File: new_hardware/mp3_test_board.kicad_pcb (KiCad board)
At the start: 4 copper layers, 100 x 56 mm, 199 parts, among them J1 TF01-A, J2 PJ-322, P1 WF24LTYAJDNN0#, P2 USB-TYPE-C-018, Q1 2N7002K, SW1 K2-1156SP-F5SW-05, SW2 K2-1156SP-F5SW-05, SW3 K2-1156SP-F5SW-05, SW4 K2-1156SP-F5SW-05, SW5 K2-1156SP-F5SW-05, SW6 GT-TC054A-H035-L1, SW7 GT-TC054A-H035-L1, SW8 GT-TC054A-H035-L1, U1 F133, U10 SGM6603-ADJYN6G, U11 SGM3204, U2 USBLC6-2SC6, U3 MX25L25645GM2I-08G, U4 PCM1795, U5 LM4562, U6 LM4562, U7 OPA1656, U8 OPA1656, U9 AXP2101, Y1 12.88727

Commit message: some fucking changes
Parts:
- removed C56, C59, C60: 0.1u, rlib_passive:C_0603_1608Metric
- removed C66: 10u, rlib_passive:C_0603_1608Metric
- removed L1, L5, L6: L, rlib_passive:INDC2520X120N
- added D13: PESD3V3L1BA, rlib_passive:D_SOD-323F, B.Cu at (123.8, 47.2)
- added D14: PESD3V3L1BA, rlib_passive:D_SOD-323F, B.Cu at (117.0, 47.0)
- added FB1: FerriteBead, rlib_passive:INDC2520X120N, B.Cu at (159.3, 48.2)
- added FB2: FerriteBead, rlib_passive:INDC2520X120N, B.Cu at (168.5, 77.6)
- added FB3: FerriteBead, rlib_passive:INDC2520X120N, B.Cu at (165.1, 62.8)
- added NT1: NetTie_2, NetTie:NetTie-2_SMD_Pad2.0mm, F.Cu at (160.1, 103.6)
- added R51: 27, rlib_passive:R_0603_1608Metric, B.Cu at (121.4, 47.0)
- added R52: 27, rlib_passive:R_0603_1608Metric, B.Cu at (119.2, 47.0)
- added R53: 10k, rlib_passive:R_0603_1608Metric, B.Cu at (105.0, 62.0)
- added R54: 0, rlib_passive:R_0603_1608Metric, B.Cu at (147.9, 45.2)
- added R55: 0, rlib_passive:R_0603_1608Metric, B.Cu at (149.8, 45.2)
- added R56: 10k, rlib_passive:R_0603_1608Metric, B.Cu at (110.6, 46.2)
- added R57: 10k, rlib_passive:R_0603_1608Metric, B.Cu at (110.6, 44.2)
- added U12: AP6212, rlib_modules:QFN-44_L12.0-W12.0-P0.90-TL_AP6212, F.Cu at (122.1, 111.0)
- C32, C33: footprint rlib_passive:R_0603_1608Metric -> rlib_passive:C_0603_1608Metric
- C34, C35, C45, C46, C55: value 0.1u -> 100n
- C51, C52, R10, R11, R7, R9: moved to B.Cu
- R47: value R -> 100k
- R48: value R -> 11k
- R6: value 50 -> 100
- moved R39 130.9 mm to (147.6, 75.8), turned to 0 degrees
- moved R35 116.2 mm to (144.8, 76.6), turned to 90 degrees
- moved R49 103.4 mm to (153.6, 49.4), turned to 0 degrees
- moved TP13 99.8 mm to (154.8, 95.2)
- moved TP15 90.8 mm to (155.6, 46.6)
- moved C52 89.4 mm to (150.4, 80.6), turned to 90 degrees
- moved C51 88.8 mm to (150.4, 76.5), turned to 90 degrees
- moved R50 85.9 mm to (152.2, 47.2), turned to 90 degrees
- moved R36 80.2 mm to (144.8, 80.7), turned to 90 degrees
- moved R40 78.9 mm to (147.7, 81.7), turned to 0 degrees
- moved R46 78.4 mm to (165.0, 69.8), turned to 0 degrees
- moved R20 74.3 mm to (164.6, 53.4)
- moved TP19 73.9 mm to (171.3, 80.8)
- moved R7 73.1 mm to (156.3, 60.0), turned to 180 degrees
- moved R19 71.6 mm to (164.7, 59.4)
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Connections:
- C16 pad 1: +0V9 -> -5VA
- C16 pad 2: GND -> GNDA
- C20 pad 1: Net-(C20-Pad1) -> GNDA
- C20 pad 2: GND -> +5VA
- C3 pad 1: +1V8A -> /SOC/KEYS
- C34 pad 1: GNDA -> -5VA
- C34 pad 2: +5VA -> GNDA
- C35 pad 1: -5VA -> GNDA
- C35 pad 2: GNDA -> +5VA
- C45 pad 1: GNDA -> -5VA
- C45 pad 2: +5VA -> GNDA
- C46 pad 1: -5VA -> GNDA
- C46 pad 2: GNDA -> +5VA
- C55 pad 1: GNDA -> -5VA
- C55 pad 2: +5VA -> GNDA
- C62 pad 1: Net-(C62-Pad1) -> VBUS
- C7 pad 1: +1V8A -> GNDA
- C7 pad 2: GND -> +5VA
- D1 pad 2: Net-(C20-Pad1) -> /SOC/KEYS
- P1 pad 22: unconnected-(P1-Pad22) -> GND
- P1 pad 30: Net-(P1-Pad30) -> /SOC/LCD_EN
- P1 pad 34: unconnected-(P1-Pad34) -> GND
- P1 pad 35: unconnected-(P1-Pad35) -> GND
- R13 pad 2: Net-(C20-Pad1) -> Net-(R13-Pad2)
- R16 pad 2: /SOC/SDC_D0 -> /SOC/SDC_CMD
- R18 pad 2: /SOC/SDC_D1 -> /SOC/SDC_CLK
- R3 pad 1: Net-(P1-Pad30) -> /SOC/LCD_EN
- SW7 pad 1: Net-(C20-Pad1) -> Net-(R13-Pad2)
- TP10 pad 1: DEBUG_UART_TX -> Net-(D14-Pad2)
- TP9 pad 1: DEBUG_UART_RX -> Net-(D13-Pad2)
- U1 pad 1: /SOC/SDC_PLUG -> unconnected-(U1-Pad1)
- U1 pad 10: unconnected-(U1-Pad10) -> /SOC/SDC_CMD
- U1 pad 11: unconnected-(U1-Pad11) -> /SOC/SDC_D3
- U1 pad 118: /SOC/SDC_CMD -> unconnected-(U1-Pad118)
- U1 pad 119: /SOC/SDC_D0 -> unconnected-(U1-Pad119)
- U1 pad 12: unconnected-(U1-Pad12) -> /SOC/SDC_D2
- U1 pad 120: /SOC/SDC_CLK -> unconnected-(U1-Pad120)
- U1 pad 121: /SOC/SDC_D1 -> unconnected-(U1-Pad121)
- U1 pad 122: /SOC/SDC_D3 -> unconnected-(U1-Pad122)
- U1 pad 123: /SOC/SDC_D2 -> unconnected-(U1-Pad123)
- U1 pad 124: /NewDAC/I2S_LRCK -> unconnected-(U1-Pad124)
- U1 pad 125: /NewDAC/I2S_BCLK -> unconnected-(U1-Pad125)
- U1 pad 127: /NewDAC/I2S_DIN -> unconnected-(U1-Pad127)
- U1 pad 2: /SOC/LCD_EN -> unconnected-(U1-Pad2)
- U1 pad 3: /NewDAC/I2C_SDIN -> unconnected-(U1-Pad3)
- U1 pad 31: /Power/IRQ -> unconnected-(U1-Pad31)
- U1 pad 32: unconnected-(U1-Pad32) -> /Power/IRQ
- U1 pad 38: unconnected-(U1-Pad38) -> /SOC/LCD_PWM
- U1 pad 4: /NewDAC/I2C_SCL -> unconnected-(U1-Pad4)
- U1 pad 47: unconnected-(U1-Pad47) -> Net-(R53-Pad1)
- U1 pad 5: /SOC/LCD_PWM -> unconnected-(U1-Pad5)
- U1 pad 52: unconnected-(U1-Pad52) -> /SOC/LCD_EN
- U1 pad 6: /NewDAC/I2S_MCLK -> /SOC/SDC_PLUG
- U1 pad 7: unconnected-(U1-Pad7) -> /SOC/SDC_D1
- U1 pad 79: unconnected-(U1-Pad79) -> /NewDAC/I2S_MCLK
- U1 pad 8: unconnected-(U1-Pad8) -> /SOC/SDC_D0
- U1 pad 80: unconnected-(U1-Pad80) -> /NewDAC/I2S_LRCK
- U1 pad 82: /SOC/LCD_D9 -> /NewDAC/I2S_BCLK
- U1 pad 84: /SOC/LCD_D8 -> /NewDAC/I2S_DIN
- U1 pad 85: /SOC/LCD_D1 -> /NewDAC/I2C_SDIN
- U1 pad 86: /SOC/LCD_D0 -> /NewDAC/I2C_SCL
- U1 pad 9: unconnected-(U1-Pad9) -> /SOC/SDC_CLK
- U9 pad 11: Net-(C66-Pad1) -> unconnected-(U9-Pad11)
- U9 pad 37: Net-(C62-Pad1) -> VBUS
- U9 pad 6: unconnected-(U9-Pad6) -> Net-(R54-Pad2)
- U9 pad 7: unconnected-(U9-Pad7) -> Net-(R55-Pad2)
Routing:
- net +5VA: track 10.3 -> 160.1 mm, vias 0 -> 10
- net /NewDAC/I2C_SDIN: track 3.83 -> 128.8 mm, vias 0 -> 6
- net -5VA: track 10.2 -> 135.1 mm, vias 0 -> 7
- net /NewDAC/I2C_SCL: track 3.30 -> 127.4 mm, vias 0 -> 6
- net /SOC/KEYS: track 36.8 -> 139.2 mm, vias 0 -> 2
- net GNDA: track 11.6 -> 113.2 mm, vias 3 -> 24
- net Net-(D12-Pad1): track 0.00 -> 99.4 mm, vias 0 -> 5
- net GND: track 90.0 -> 189.1 mm, vias 49 -> 81
- net +0V9: track 216.0 -> 139.6 mm, vias 4 -> 7
- net /SOC/USB_DM: track 53.6 -> 118.5 mm, vias 2 -> 4
- net /SOC/USB_DP: track 55.5 -> 112.1 mm, vias 2 -> 4
- net +3V3: track 296.9 -> 351.6 mm, vias 18 -> 20
- net Net-(C49-Pad2): track 10.1 -> 52.9 mm, vias 0 -> 2
- net VBUS: track 0.00 -> 42.6 mm, vias 0 -> 3
- net VCC: track 11.3 -> 49.0 mm, vias 0 -> 4
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- added copper zone on B.Cu, net +0V9
- added copper zone on B.Cu, net +3V3
- added copper zone on B.Cu, net GND
- added copper zone on In2.Cu, net GNDA

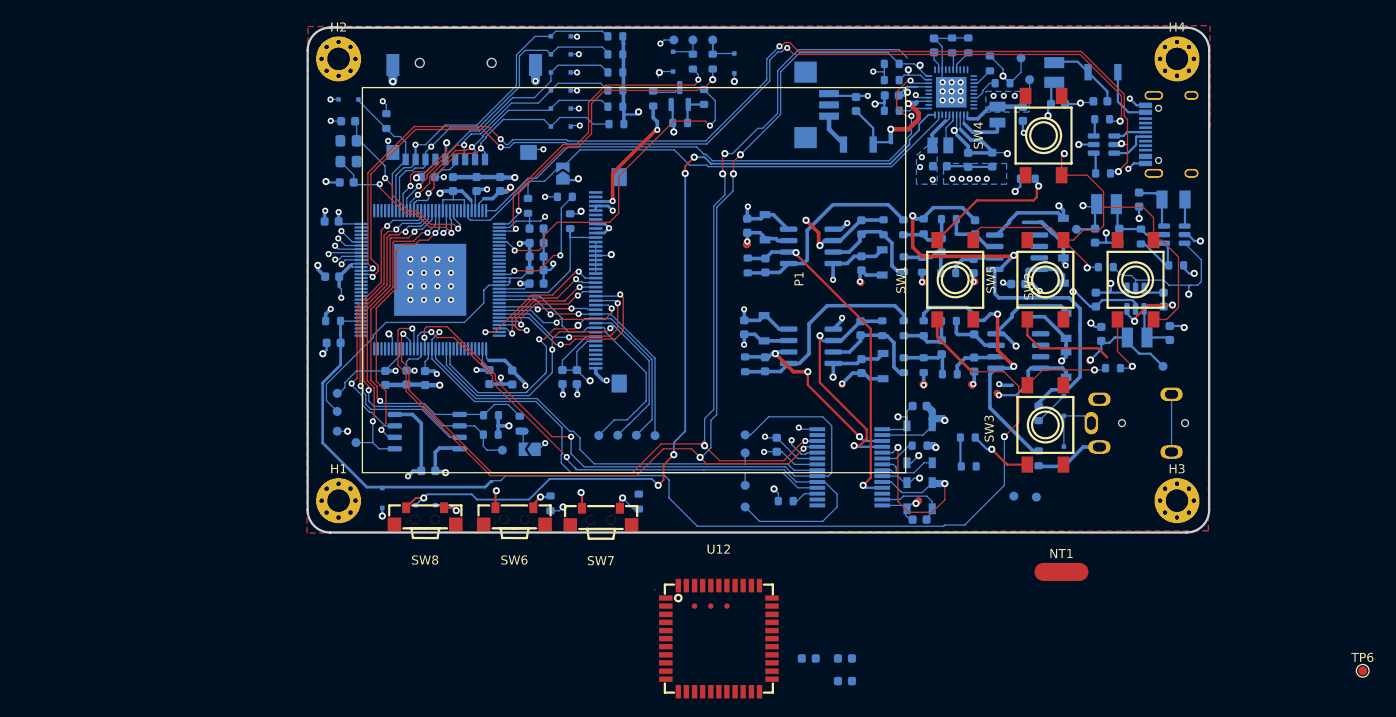
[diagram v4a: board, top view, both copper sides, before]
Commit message: device tree is changed
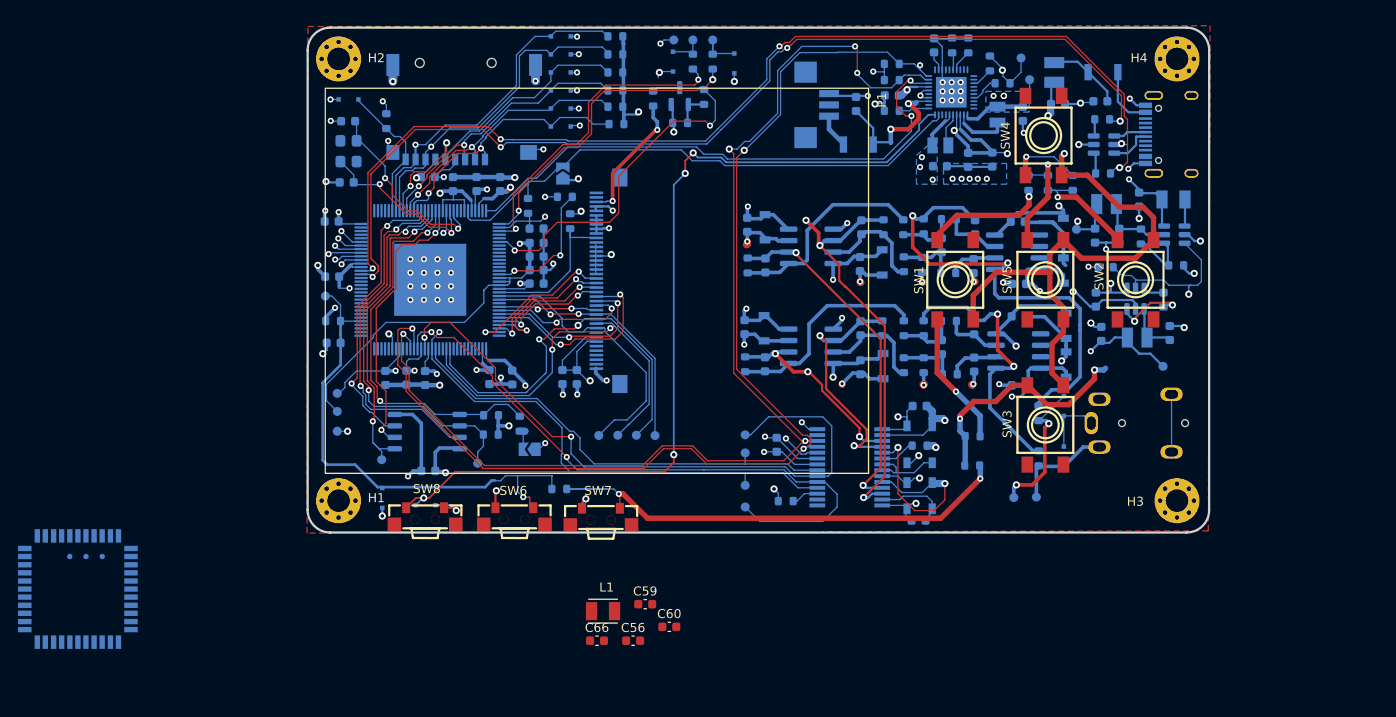
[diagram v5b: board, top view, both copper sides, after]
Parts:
- removed NT1: NetTie_2, NetTie:NetTie-2_SMD_Pad2.0mm
- added C56: 10u, rlib_passive:C_0603_1608Metric, F.Cu at (112.6, 111.2)
- added C59: 10u, rlib_passive:C_0603_1608Metric, F.Cu at (113.9, 107.2)
- added C60: 10u, rlib_passive:C_0603_1608Metric, F.Cu at (116.6, 109.7)
- added C66: 100n, rlib_passive:C_0603_1608Metric, F.Cu at (108.6, 111.2)
- added L1: 4.7u, rlib_passive:IND_LQH32PN4R7NN0L, F.Cu at (109.2, 108.0)
- R41, R42: value 50 -> 51
- TP6: moved to B.Cu
- U: renamed from U12; moved to B.Cu
- moved TP6 122.3 mm to (78.4, 73.0), turned to 180 degrees
- moved U 71.3 mm to (51.0, 105.5), turned to 180 degrees
- moved R12 65.6 mm to (158.6, 60.5), turned to -90 degrees
- moved R7 62.3 mm to (104.4, 94.4), turned to 0 degrees
- moved R13 59.7 mm to (161.3, 60.5), turned to 90 degrees
- moved C16 49.3 mm to (125.2, 65.1), turned to -90 degrees
- moved C7 44.1 mm to (137.7, 69.5), turned to 90 degrees
- moved C20 34.9 mm to (137.8, 80.9), turned to 90 degrees
- moved R11 32.1 mm to (156.4, 60.5), turned to 90 degrees
- moved C46 31.1 mm to (155.3, 82.9), turned to 0 degrees
- moved C35 30.8 mm to (155.4, 71.7), turned to 0 degrees
- moved C45 23.6 mm to (155.2, 64.8), turned to 0 degrees
- moved R9 19.0 mm to (150.2, 91.8)
- moved C34 14.8 mm to (124.9, 76.5), turned to -90 degrees
- moved P1 4.12 mm to (138.7, 92.7)
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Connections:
- C16 pad 2: GNDA -> GND
- C20 pad 1: GNDA -> GND
- C29 pad 2: GNDA -> GND
- C30 pad 1: GNDA -> GND
- C32 pad 2: GNDA -> GND
- C33 pad 2: GNDA -> GND
- C34 pad 2: GNDA -> GND
- C35 pad 1: GNDA -> GND
- C36 pad 2: GNDA -> GND
- C37 pad 2: GNDA -> GND
- C38 pad 2: GNDA -> GND
- C39 pad 2: GNDA -> GND
- C40 pad 1: GNDA -> GND
- C45 pad 2: GNDA -> GND
- C46 pad 1: GNDA -> GND
- C50 pad 1: GNDA -> GND
- C52 pad 1: GNDA -> GND
- C53 pad 2: GNDA -> GND
- C54 pad 1: GNDA -> GND
- C55 pad 2: GNDA -> GND
- C57 pad 2: GNDA -> GND
- C58 pad 1: GNDA -> GND
- C69 pad 2: GNDA -> GND
- C7 pad 1: GNDA -> GND
- C70 pad 2: GNDA -> GND
- C72 pad 2: GNDA -> GND
- C73 pad 2: GNDA -> GND
- C74 pad 2: GNDA -> GND
- C75 pad 2: GNDA -> GND
- D10 pad 1: GNDA -> GND
- D9 pad 1: GNDA -> GND
- J2 pad 1: GNDA -> GND
- P1 pad 40: (no net) -> unconnected-(P1-Pad40)
- R24 pad 2: GNDA -> GND
- R34 pad 1: GNDA -> GND
- R36 pad 1: GNDA -> GND
- R48 pad 1: GNDA -> GND
- SW1 pad 1: /SOC/KEYS -> Net-(R10-Pad2)
- SW1 pad 2: /SOC/KEYS -> Net-(R10-Pad2)
- SW1 pad 4: GND -> unconnected-(SW1-Pad4)
- SW2 pad 1: Net-(R7-Pad2) -> Net-(R12-Pad2)
- SW2 pad 2: Net-(R7-Pad2) -> Net-(R12-Pad2)
- SW3 pad 4: GND -> unconnected-(SW3-Pad4)
- SW4 pad 1: Net-(R10-Pad2) -> Net-(R13-Pad2)
- SW4 pad 2: Net-(R10-Pad2) -> Net-(R13-Pad2)
- SW6 pad 1: Net-(R12-Pad2) -> /SOC/KEYS
- SW7 pad 1: Net-(R13-Pad2) -> Net-(R7-Pad2)
- U pad 1: unconnected-(U12-Pad1) -> GND
- U pad 14: unconnected-(U12-Pad14) -> /SOC/WIFI_SDIO_D2
- U pad 15: unconnected-(U12-Pad15) -> /SOC/WIFI_SDIO_D3
- U pad 16: unconnected-(U12-Pad16) -> /SOC/WIFI_SDIO_CMD
- U pad 17: unconnected-(U12-Pad17) -> /SOC/WIFI_SDIO_CLK
- U pad 18: unconnected-(U12-Pad18) -> /SOC/WIFI_SDIO_D0
- U pad 19: unconnected-(U12-Pad19) -> /SOC/WIFI_SDIO_D1
- U pad 20: unconnected-(U12-Pad20) -> GND
- U pad 21: unconnected-(U12-Pad21) -> Net-(L1-Pad1)
- U pad 22: unconnected-(U12-Pad22) -> +3V3
- U pad 23: unconnected-(U12-Pad23) -> +3V3
- U pad 3: unconnected-(U12-Pad3) -> GND
- U pad 31: unconnected-(U12-Pad31) -> GND
- U pad 33: unconnected-(U12-Pad33) -> GND
- U pad 36: unconnected-(U12-Pad36) -> GND
- U pad 9: unconnected-(U12-Pad9) -> +3V3
- U1 pad 118: unconnected-(U1-Pad118) -> /SOC/WIFI_SDIO_CMD
- U1 pad 119: unconnected-(U1-Pad119) -> /SOC/WIFI_SDIO_D0
- U1 pad 120: unconnected-(U1-Pad120) -> /SOC/WIFI_SDIO_CLK
- U1 pad 121: unconnected-(U1-Pad121) -> /SOC/WIFI_SDIO_D1
- U1 pad 122: unconnected-(U1-Pad122) -> /SOC/WIFI_SDIO_D2
- U1 pad 123: unconnected-(U1-Pad123) -> /SOC/WIFI_SDIO_D3
- U1 pad 74: /SOC/AUDIO_PWR_EN -> /Power/AUDIO_PWR_EN
- U10 pad 2: GNDA -> GND
- U11 pad 4: GNDA -> GND
- U4 pad 16: GNDA -> GND
- U4 pad 19: GNDA -> GND
- U4 pad 24: GNDA -> GND
- U4 pad 27: GNDA -> GND
- U5 pad 3: GNDA -> GND
- U5 pad 5: GNDA -> GND
- U6 pad 3: GNDA -> GND
- U6 pad 5: GNDA -> GND
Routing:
- net GND: track 189.1 -> 312.5 mm, vias 81 -> 106
- net GNDA: track 113.2 -> 0.00 mm, vias 24 -> 0
- net /SOC/KEYS: track 139.2 -> 56.1 mm, vias 2 -> 1
- net Net-(R7-Pad2): track 8.93 -> 56.6 mm
- net Net-(C44-Pad1): track 11.7 -> 45.9 mm, vias 2 -> 3
- net Net-(R10-Pad2): track 3.24 -> 28.1 mm, vias 0 -> 2
- net -5VA: track 135.1 -> 151.8 mm, vias 7 -> 5
- net VCC: track 49.0 -> 65.5 mm, vias 4 -> 5
- net Net-(D10-Pad2): track 10.3 -> 22.4 mm, vias 0 -> 2
- net Net-(R12-Pad2): track 2.67 -> 13.2 mm
- net Net-(R10-Pad1): track 16.5 -> 26.6 mm
- net Net-(R13-Pad2): track 3.58 -> 8.09 mm
- net unconnected-(U1-Pad120): track 3.67 -> 0.00 mm, vias 1 -> 0
- net /SOC/WIFI_SDIO_CLK: track 0.00 -> 3.67 mm, vias 0 -> 1
- net Net-(D9-Pad2): track 7.67 -> 11.2 mm
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- removed copper zone on In2.Cu, net GNDA

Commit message: software
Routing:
- net /SOC/SDC_CLK: track 35.4 -> 34.4 mm
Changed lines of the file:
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@@
   (segment (start 92.26 64.421084) (end 92.26 63.5375) (width 0.127) (layer "B.Cu") (net 4))
   (segment (start 92.415579 66.004111) (end 92.415579 64.576663) (width 0.127) (layer "B.Cu") (net 4))
-  (segment (start 84.4678 60.592797) (end 84.414092 60.592797) (width 0.127) (layer "B.Cu") (net 4))
+  (segment (start 84.4678 60.592797) (end 84.178941 60.303938) (width 0.127) (layer "B.Cu") (net 4))
+  (segment (start 84.178941 60.303938) (end 81.671062 60.303938) (width 0.127) (layer "B.Cu") (net 4))
   (segment (start 81.575 59.56448) (end 80.098977 58.088457) (width 0.127) (layer "B.Cu") (net 4))
-  (segment (start 81.822 60.647) (end 81.575 60.4) (width 0.127) (layer "B.Cu") (net 4))
-  (segment (start 84.359889 60.647) (end 81.822 60.647) (width 0.127) (layer "B.Cu") (net 4))
-  (segment (start 84.414092 60.592797) (end 84.359889 60.647) (width 0.127) (layer "B.Cu") (net 4))
+  (segment (start 81.671062 60.303938) (end 81.575 60.4) (width 0.127) (layer "B.Cu") (net 4))
   (segment (start 92.415579 64.576663) (end 92.26 64.421084) (width 0.127) (layer "B.Cu") (net 4))
   (segment (start 81.575 60.4) (end 81.575 59.56448) (width 0.127) (layer "B.Cu") (net 4))
@@
   (via (at 91.8827 56.003938) (size 0.8) (drill 0.4) (layers "F.Cu" "B.Cu") (net 21))
   (via (at 87.8827 60.803938) (size 0.6858) (drill 0.3302) (layers "F.Cu" "B.Cu") (net 21))
-  (segment (start 103.45 49.17288) (end 103.45 48.2) (width 0.127) (layer "B.Cu") (net 21))
   (segment (start 87.06 63.5375) (end 87.06 61.626638) (width 0.127) (layer "B.Cu") (net 21))
   (segment (start 87.06 61.626638) (end 87.8827 60.803938) (width 0.127) (layer "B.Cu") (net 21))
   (segment (start 104.25 47.4) (end 103.681224 47.968776) (width 0.127) (layer "B.Cu") (net 21))
+  (segment (start 103.45 49.17288) (end 103.45 48.2) (width 0.127) (layer "B.Cu") (net 21))
+  (segment (start 95.518065 54.693469) (end 99.211534 51) (width 0.127) (layer "B.Cu") (net 21))
   (segment (start 91.7398 57.8488) (end 91.7398 56.146838) (width 0.127) (layer "B.Cu") (net 21))
+  (segment (start 91.7398 56.146838) (end 93.193169 54.693469) (width 0.127) (layer "B.Cu") (net 21))
+  (segment (start 93.193169 54.693469) (end 95.518065 54.693469) (width 0.127) (layer "B.Cu") (net 21))
+  (segment (start 99.211534 51) (end 101.62288 51) (width 0.127) (layer "B.Cu") (net 21))
   (segment (start 101.62288 51) (end 103.45 49.17288) (width 0.127) (layer "B.Cu") (net 21))
-  (segment (start 99.211534 51) (end 101.62288 51) (width 0.127) (layer "B.Cu") (net 21))
   (segment (start 108.975 47.4) (end 104.25 47.4) (width 0.127) (layer "B.Cu") (net 21))
   (segment (start 109.775 48.2) (end 108.975 47.4) (width 0.127) (layer "B.Cu") (net 21))
-  (segment (start 91.7398 57.430863) (end 94.477194 54.693469) (width 0.127) (layer "B.Cu") (net 21))
-  (segment (start 91.7398 57.8488) (end 91.7398 57.430863) (width 0.127) (layer "B.Cu") (net 21))
-  (segment (start 95.518065 54.693469) (end 99.211534 51) (width 0.127) (layer "B.Cu") (net 21))
-  (segment (start 94.477194 54.693469) (end 95.518065 54.693469) (width 0.127) (layer "B.Cu") (net 21))
   (segment (start 91.7398 56.146838) (end 91.8827 56.003938) (width 0.127) (layer "B.Cu") (net 21))
   (segment (start 93.036638 56.25) (end 93.83 56.25) (width 0.127) (layer "F.Cu") (net 22))
@@
   (via (at 89.8827 61.603938) (size 0.6858) (drill 0.3302) (layers "F.Cu" "B.Cu") (net 24))
   (via (at 95.687115 56.621476) (size 0.6858) (drill 0.3302) (layers "F.Cu" "B.Cu") (net 24))
-  (segment (start 95.687115 56.038444) (end 96.243122 55.482437) (width 0.127) (layer "B.Cu") (net 24))
-  (segment (start 95.687115 56.621476) (end 95.687115 56.038444) (width 0.127) (layer "B.Cu") (net 24))
   (segment (start 104.45 53.2) (end 107.385 53.2) (width 0.127) (layer "B.Cu") (net 24))
   (segment (start 89.2827 62.403938) (end 89.6827 62.403938) (width 0.127) (layer "B.Cu") (net 24))
   (segment (start 89.8827 62.203938) (end 89.8827 61.603938) (width 0.127) (layer "B.Cu") (net 24))
   (segment (start 88.26 63.5375) (end 88.26 62.689086) (width 0.127) (layer "B.Cu") (net 24))
+  (segment (start 95.687115 56.621476) (end 95.687115 56.038444) (width 0.127) (layer "B.Cu") (net 24))
   (segment (start 88.438864 62.560102) (end 88.595028 62.403938) (width 0.127) (layer "B.Cu") (net 24))
   (segment (start 109.895 53.93) (end 108.2 53.93) (width 0.127) (layer "B.Cu") (net 24))
@@
   (segment (start 96.1398 57.074161) (end 96.1398 57.8488) (width 0.127) (layer "B.Cu") (net 24))
   (segment (start 89.2827 62.403938) (end 89.4827 62.403938) (width 0.127) (layer "B.Cu") (net 24))
+  (segment (start 88.26 62.689086) (end 88.334 62.615086) (width 0.127) (layer "B.Cu") (net 24))
+  (segment (start 95.687115 56.038444) (end 98.305559 53.42) (width 0.127) (layer "B.Cu") (net 24))
+  (segment (start 107.385 53.2) (end 108.125 53.94) (width 0.127) (layer "B.Cu") (net 24))
   (segment (start 102.67 53.42) (end 103.45 54.2) (width 0.127) (layer "B.Cu") (net 24))
-  (segment (start 88.26 62.689086) (end 88.334 62.615086) (width 0.127) (layer "B.Cu") (net 24))
-  (segment (start 107.385 53.2) (end 108.125 53.94) (width 0.127) (layer "B.Cu") (net 24))
-  (segment (start 98.178878 53.42) (end 102.67 53.42) (width 0.127) (layer "B.Cu") (net 24))
   (segment (start 88.595028 62.403938) (end 89.2827 62.403938) (width 0.127) (layer "B.Cu") (net 24))
   (segment (start 95.687115 56.621476) (end 96.1398 57.074161) (width 0.127) (layer "B.Cu") (net 24))
+  (segment (start 98.305559 53.42) (end 102.67 53.42) (width 0.127) (layer "B.Cu") (net 24))
   (segment (start 103.45 54.2) (end 104.45 53.2) (width 0.127) (layer "B.Cu") (net 24))
-  (segment (start 96.243122 55.355756) (end 98.178878 53.42) (width 0.127) (layer "B.Cu") (net 24))
-  (segment (start 96.243122 55.482437) (end 96.243122 55.355756) (width 0.127) (layer "B.Cu") (net 24))
   (segment (start 85.86 63.5375) (end 85.86 59.426638) (width 0.127) (layer "B.Cu") (net 25))
   (segment (start 86.71 55.31) (end 86.085 55.31) (width 0.127) (layer "B.Cu") (net 25))
